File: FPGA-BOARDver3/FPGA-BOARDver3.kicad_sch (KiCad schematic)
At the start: 0 parts

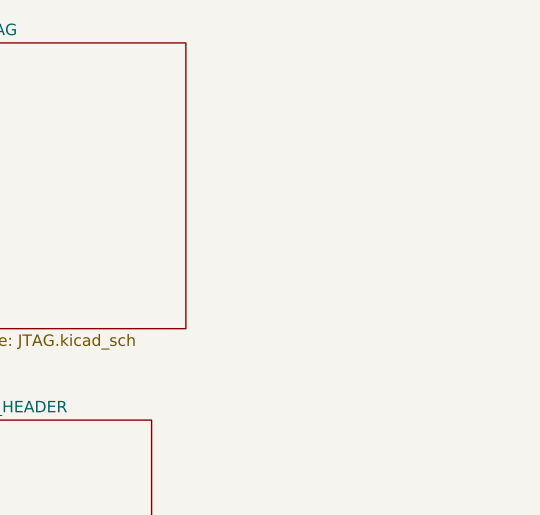
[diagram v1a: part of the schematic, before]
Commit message: added audio out and usb
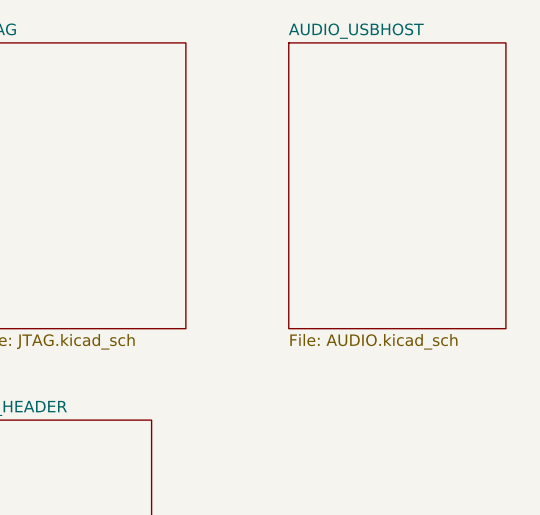
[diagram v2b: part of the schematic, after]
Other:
- added sheet AUDIO_USBHOST (AUDIO.kicad_sch)
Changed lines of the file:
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@@
+	)
+	(sheet
+		(at 123.19 19.05)
+		(size 24.13 31.75)
+		(fields_autoplaced yes)
+		(stroke
+			(width 0.1524)
+			(type solid)
+		)
+		(fill
+			(color 0 0 0 0.0000)
+		)
+		(property "Sheetname" "AUDIO_USBHOST"
+			(at 123.19 18.3384 0)
+			(effects
+				(font
+					(size 1.27 1.27)
+				)
+				(justify left bottom)
+			)
+		)
+		(property "Sheetfile" "AUDIO.kicad_sch"
+			(at 123.19 51.3846 0)
+			(effects
+				(font
+					(size 1.27 1.27)
+				)
+				(justify left top)
+			)
+		)
+		(instances
+			(project "FPGA-BOARDver3"
+				(path "/4a327bdf-04e5-4836-9c0a-5fb801c23f64"
+					(page "14")
+				)
+			)
+		)
 	)
 	(sheet

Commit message: updated schematic and layout
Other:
- added sheet USB_JTAG_PROGRAMMING (USB_JTAG_PROGRAMMING.kicad_sch)
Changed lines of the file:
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@@
+	)
+	(sheet
+		(at 123.19 62.23)
+		(size 21.59 26.67)
+		(fields_autoplaced yes)
+		(stroke
+			(width 0.1524)
+			(type solid)
+		)
+		(fill
+			(color 0 0 0 0.0000)
+		)
+		(property "Sheetname" "USB_JTAG_PROGRAMMING"
+			(at 123.19 61.5184 0)
+			(effects
+				(font
+					(size 1.27 1.27)
+				)
+				(justify left bottom)
+			)
+		)
+		(property "Sheetfile" "USB_JTAG_PROGRAMMING.kicad_sch"
+			(at 123.19 89.4846 0)
+			(effects
+				(font
+					(size 1.27 1.27)
+				)
+				(justify left top)
+			)
+		)
+		(instances
+			(project "FPGA-BOARDver3"
+				(path "/4a327bdf-04e5-4836-9c0a-5fb801c23f64"
+					(page "15")
+				)
+			)
+		)
 	)
 	(sheet
